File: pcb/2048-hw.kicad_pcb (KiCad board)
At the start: 2 copper layers, 60 x 93 mm, 102 parts, among them J1 UJC-HP-3-SMT-TR, J2 Battery, J3 SWD, SW1 SW_SPDT, SW2 PUSH_A, SW3 PUSH_B, U1 STM32F303K8Tx, U2 MCP73831-2-OT, U3 AP2210N-3.3TRG1, U4 PSP_1000_JSTK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

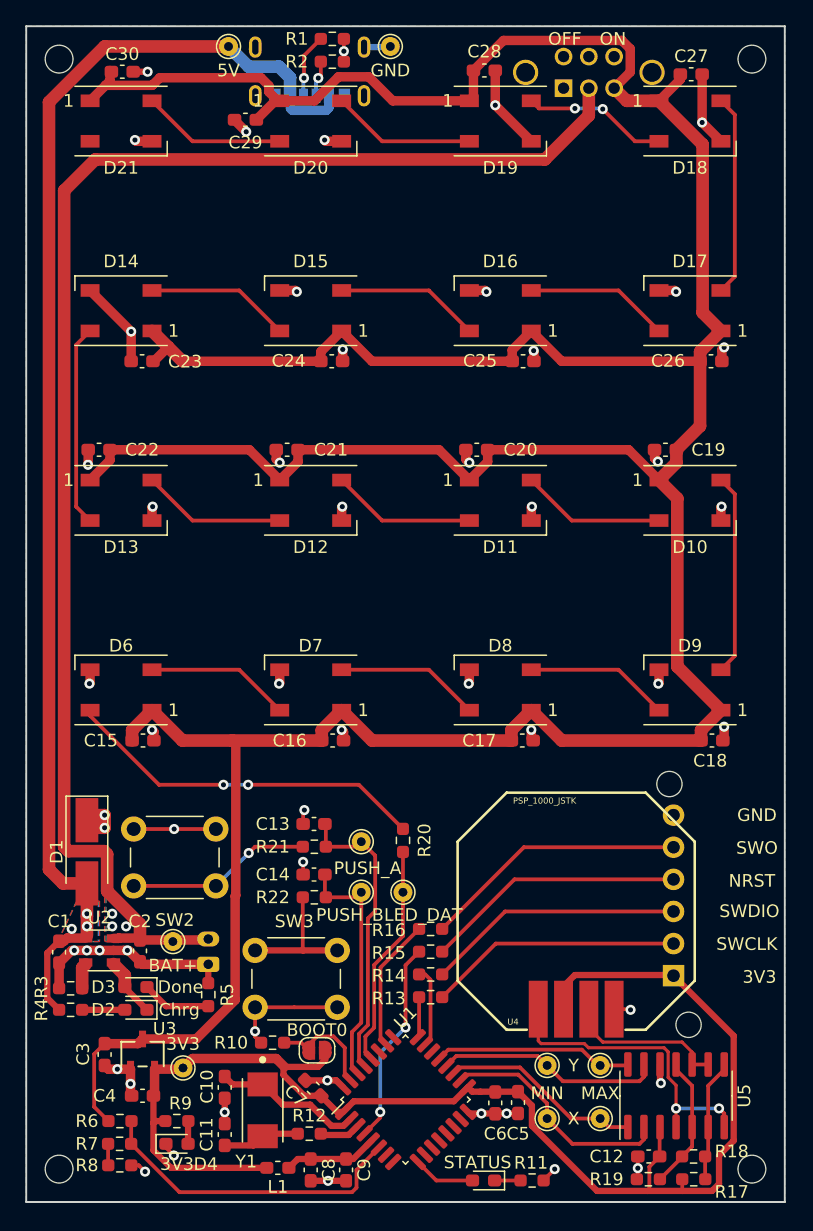
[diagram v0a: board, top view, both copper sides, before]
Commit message: Round off board corners
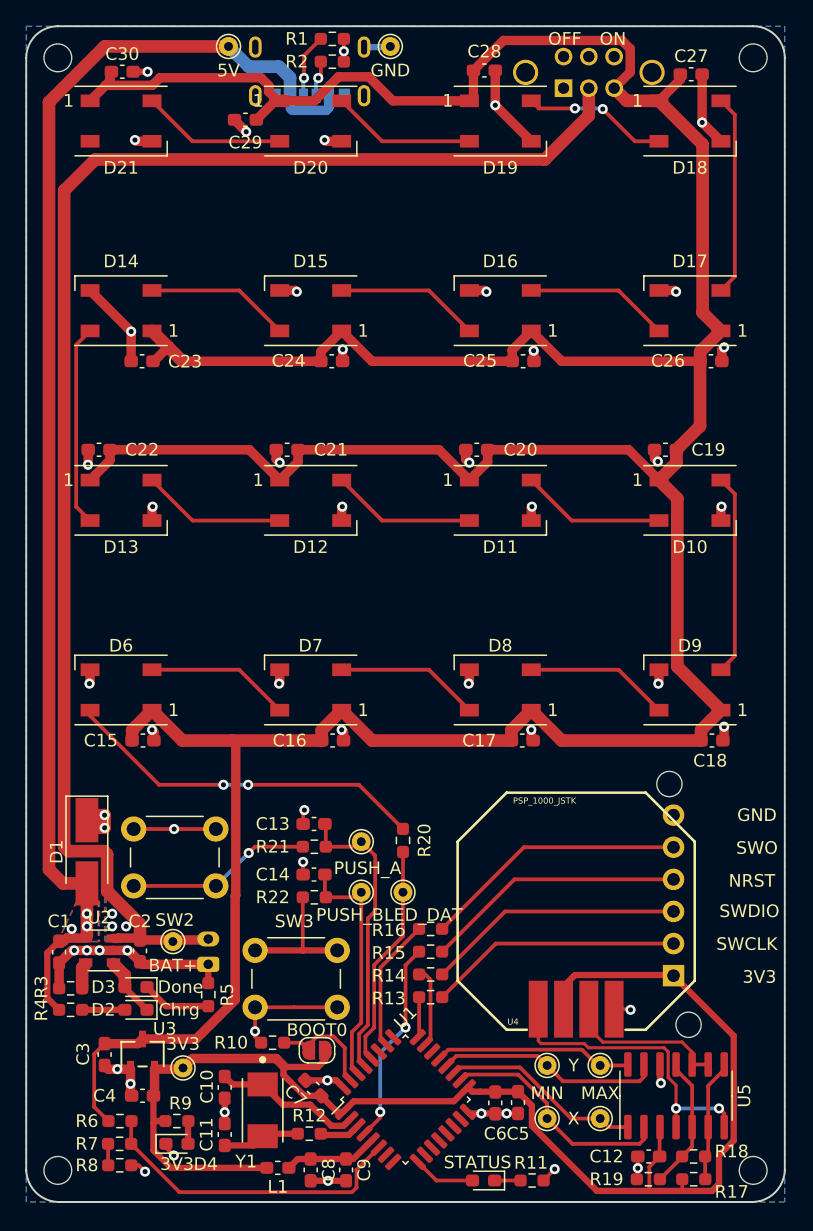
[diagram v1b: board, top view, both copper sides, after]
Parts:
- moved H1 0.14 mm to (122.5, 62.5)
- moved H3 0.14 mm to (177.5, 62.5)
- moved H2 0.14 mm to (122.5, 150.5)
- moved H4 0.14 mm to (177.5, 150.5)
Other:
- outline, holes or cut-outs redrawn
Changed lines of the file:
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@@
   (general
     (thickness 1.6)
-    (drawings 19)
+    (drawings 23)
     (tracks 594)
     (zones 0)
@@
   )
   (setup
-    (last_trace_width 0.3)
+    (last_trace_width 0.25)
     (user_trace_width 0.3)
     (user_trace_width 0.5)
@@
   )
   (module MountingHole:MountingHole_2.2mm_M2 (layer F.Cu)
-    (at 177.4 150.4)
+    (at 177.5 150.5)
     (descr "Mounting Hole 2.2mm, no annular, M2")
     (tags "mounting hole 2.2mm no annular m2")
@@
   )
   (module MountingHole:MountingHole_2.2mm_M2 (layer F.Cu)
-    (at 177.4 62.6)
+    (at 177.5 62.5)
     (descr "Mounting Hole 2.2mm, no annular, M2")
     (tags "mounting hole 2.2mm no annular m2")
@@
   )
   (module MountingHole:MountingHole_2.2mm_M2 (layer F.Cu)
-    (at 122.6 150.4)
+    (at 122.5 150.5)
     (descr "Mounting Hole 2.2mm, no annular, M2")
     (tags "mounting hole 2.2mm no annular m2")
@@
   )
   (module MountingHole:MountingHole_2.2mm_M2 (layer F.Cu)
-    (at 122.6 62.6)
+    (at 122.5 62.5)
     (descr "Mounting Hole 2.2mm, no annular, M2")
     (tags "mounting hole 2.2mm no annular m2")
@@
     )
   )
+  (gr_arc (start 122.5 62.5) (end 122.5 60) (angle -90) (layer Edge.Cuts) (width 0.15))
+  (gr_arc (start 177.5 62.5) (end 180 62.5) (angle -90) (layer Edge.Cuts) (width 0.15))
+  (gr_arc (start 122.6 150.4) (end 120 150.5) (angle -85.59480368) (layer Edge.Cuts) (width 0.15))
+  (gr_arc (start 177.4 150.4) (end 177.5 153) (angle -85.59480368) (layer Edge.Cuts) (width 0.15))
   (gr_text GND (at 177.8 122.4) (layer F.SilkS)
     (effects (font (size 1 1) (thickness 0.15)))
@@
     (effects (font (size 1 1) (thickness 0.15)))
   )
-  (gr_line (start 180 153) (end 120 153) (layer Edge.Cuts) (width 0.15))
-  (gr_line (start 180 60) (end 180 153) (layer Edge.Cuts) (width 0.15))
-  (gr_line (start 120 60) (end 180 60) (layer Edge.Cuts) (width 0.15))
-  (gr_line (start 120 153) (end 120 60) (layer Edge.Cuts) (width 0.15))
+  (gr_line (start 177.5 153) (end 122.5 153) (layer Edge.Cuts) (width 0.15))
+  (gr_line (start 180 62.5) (end 180 150.5) (layer Edge.Cuts) (width 0.15))
+  (gr_line (start 122.5 60) (end 177.5 60) (layer Edge.Cuts) (width 0.15))
+  (gr_line (start 120 150.5) (end 120 62.5) (layer Edge.Cuts) (width 0.15))
   (gr_line (start 180 120) (end 120 120) (layer Dwgs.User) (width 0.15))
   (segment (start 140.9 66.5) (end 140.9 65.5) (width 0.75) (layer B.Cu) (net 1))
@@
   (segment (start 138.1 137.6) (end 141.2 137.6) (width 0.3) (layer F.Cu) (net 2))
   (segment (start 128.5 123.5) (end 131.7 123.5) (width 0.3) (layer F.Cu) (net 2))
-  (via (at 137.4 68.35) (size 0.8) (drill 0.4) (layers F.Cu B.Cu) (net 2))
-  (segment (start 136.475 67.425) (end 137.4 68.35) (width 0.75) (layer F.Cu) (net 2))
-  (segment (start 136.475 67.4) (end 136.475 67.425) (width 0.75) (layer F.Cu) (net 2))
   (via (at 128.6 69) (size 0.8) (drill 0.4) (layers F.Cu B.Cu) (net 2))
   (segment (start 128.7 69.1) (end 128.6 69) (width 0.75) (layer F.Cu) (net 2))
@@
   (segment (start 168.375 150.325) (end 168.375 151.125) (width 0.3) (layer F.Cu) (net 2))
   (via (at 168.375 150.325) (size 0.8) (drill 0.4) (layers F.Cu B.Cu) (net 2))
+  (segment (start 136.475 67.4) (end 136.475 67.425) (width 0.75) (layer F.Cu) (net 2) (status 1000000))
+  (segment (start 136.475 67.425) (end 137.4 68.35) (width 0.75) (layer F.Cu) (net 2) (status 1000000))
+  (via (at 137.4 68.35) (size 0.8) (drill 0.4) (layers F.Cu B.Cu) (net 2) (status 1000000))
   (segment (start 128.849999 132.124999) (end 129 132.275) (width 0.75) (layer F.Cu) (net 3))
   (segment (start 127.331484 132.124999) (end 128.849999 132.124999) (width 0.75) (layer F.Cu) (net 3))
@@
   (segment (start 155.375 65.575) (end 155.05 65.9) (width 0.75) (layer F.Cu) (net 4))
   (segment (start 155.375 63.5) (end 155.375 65.575) (width 0.75) (layer F.Cu) (net 4))
-  (segment (start 139.7 65.9) (end 138.2 67.4) (width 0.75) (layer F.Cu) (net 4))
-  (segment (start 140.05 65.9) (end 139.7 65.9) (width 0.75) (layer F.Cu) (net 4))
   (segment (start 126.625 63.5) (end 126.625 64.325) (width 0.75) (layer F.Cu) (net 4))
   (segment (start 173.3 91.625) (end 171.425 93.5) (width 1) (layer F.Cu) (net 4))
@@
   (segment (start 139.9 65.9) (end 139.19501 65.19501) (width 0.75) (layer F.Cu) (net 4))
   (segment (start 126.625 64.325) (end 126.275 64.675) (width 0.75) (layer F.Cu) (net 4))
+  (segment (start 140.05 65.9) (end 139.7 65.9) (width 0.75) (layer F.Cu) (net 4) (status 1000000))
+  (segment (start 139.7 65.9) (end 138.2 67.4) (width 0.75) (layer F.Cu) (net 4) (status 1000000))
   (segment (start 144.582152 145.872272) (end 143.30988 144.6) (width 0.5) (layer F.Cu) (net 5))
   (segment (start 145.06793 145.872272) (end 144.582152 145.872272) (width 0.5) (layer F.Cu) (net 5))
@@
   (segment (start 171.8875 151.2) (end 171.8875 152.1125) (width 0.3) (layer F.Cu) (net 5))
   (segment (start 171.87499 152.12501) (end 174.247278 152.12501) (width 0.5) (layer F.Cu) (net 5))
+  (segment (start 169.12501 152.12501) (end 171.87499 152.12501) (width 0.5) (layer F.Cu) (net 5))
+  (segment (start 165.149008 152.12501) (end 169.12501 152.12501) (width 0.5) (layer F.Cu) (net 5))
   (segment (start 169.28749 151.96253) (end 169.12501 152.12501) (width 0.3) (layer F.Cu) (net 5))
   (segment (start 169.28749 150.21251) (end 169.28749 151.96253) (width 0.3) (layer F.Cu) (net 5))
   (segment (start 170.1 149.4) (end 169.28749 150.21251) (width 0.3) (layer F.Cu) (net 5))
-  (segment (start 169.12501 152.12501) (end 171.87499 152.12501) (width 0.5) (layer F.Cu) (net 5))
-  (segment (start 165.149008 152.12501) (end 169.12501 152.12501) (width 0.5) (layer F.Cu) (net 5))
   (segment (start 145.865686 149.6) (end 147.330672 148.135014) (width 0.5) (layer F.Cu) (net 6))
   (segment (start 145.3 149.6) (end 145.865686 149.6) (width 0.5) (layer F.Cu) (net 6))
@@
   (segment (start 148.15 69.1) (end 144.95 65.9) (width 0.3) (layer F.Cu) (net 29))
   (segment (start 155.05 69.1) (end 148.15 69.1) (width 0.3) (layer F.Cu) (net 29))
-  (segment (start 133.15 69.1) (end 129.95 65.9) (width 0.3) (layer F.Cu) (net 30))
-  (segment (start 140.05 69.1) (end 133.15 69.1) (width 0.3) (layer F.Cu) (net 30))
+  (segment (start 140.05 69.1) (end 133.15 69.1) (width 0.3) (layer F.Cu) (net 30) (status 1000000))
+  (segment (start 133.15 69.1) (end 129.95 65.9) (width 0.3) (layer F.Cu) (net 30) (status 1000000))
   (via (at 143.1 64.1) (size 0.8) (drill 0.4) (layers F.Cu B.Cu) (net 32))
   (segment (start 143.3 63.9) (end 143.1 64.1) (width 0.3) (layer F.Cu) (net 32))

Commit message: Use shorter power switch
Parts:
- SW1: footprint 2048-hw:E_SWITCH_EG2208A -> 2048-hw:E_SWITCH_EG2208

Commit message: Tidy up silkscreen and traces
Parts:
- D10, D11, D12, D13, D14, D15, D16, D17, D18, D19, D20, D21, D6, D7, D8, D9: footprint LED_SMD:LED_WS2812B_PLCC4_5.0x5.0mm_P3.2mm -> 2048-hw:LED_WS2812B_PLCC4_5.0x5.0mm_P3.2mm_no1
- moved C8 1.10 mm to (143.6, 150.5)
- moved D5 0.65 mm to (155.5, 151.3)
- turned C15 to 180 degrees
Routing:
- net Net-(R22-Pad2): track 17.2 -> 10.7 mm
- net GND: track 116.8 -> 120.6 mm, vias 53 -> 52
- net V_BAT: track 319.8 -> 319.0 mm
- net Net-(D5-Pad1): track 2.05 -> 2.70 mm
- net LED_STATUS: track 4.94 -> 4.29 mm
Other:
- board text added: "+"
- board text added: "-"
- board text added: "2048-hw"
- board text added: "Rev 1.0 | Christopher Hall"

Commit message: Reverse the backwards zener diode
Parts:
- turned D1 to 90 degrees
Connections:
- D1 pad 1: GND -> +5V
- D1 pad 2: +5V -> GND

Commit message: Update component values for BOM
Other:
- board text added: "JLCJLCJLCJLC"
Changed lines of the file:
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@@
   (general
     (thickness 1.6)
-    (drawings 36)
+    (drawings 37)
     (tracks 594)
     (zones 0)
@@
       (usegerberattributes true)
       (usegerberadvancedattributes true)
-      (creategerberjobfile true)
+      (creategerberjobfile false)
       (excludeedgelayer true)
       (linewidth 0.100000)
@@
       (outputformat 1)
       (mirror false)
-      (drillshape 1)
+      (drillshape 0)
       (scaleselection 1)
-      (outputdirectory ""))
+      (outputdirectory "gerber/"))
   )
   (net 0 "")
@@
       (effects (font (size 1 1) (thickness 0.15)) (justify mirror))
     )
-    (pad 1 thru_hole roundrect (at 0 0 90) (size 1.2 1.75) (drill 0.75) (layers *.Cu *.Mask) (roundrect_rratio 0.208333)
+    (pad 1 thru_hole roundrect (at 0 0 90) (size 1.2 1.75) (drill 0.75) (layers *.Cu *.Mask) (roundrect_rratio 0.2083325)
       (net 2 GND))
     (pad 2 thru_hole oval (at 2 0 90) (size 1.2 1.75) (drill 0.75) (layers *.Cu *.Mask)
@@
     )
   )
+  (gr_text JLCJLCJLCJLC (at 149.8 145) (layer F.SilkS)
+    (effects (font (size 0.7 0.7) (thickness 0.1)))
+  )
   (gr_circle (center 127.9 134.1) (end 128 134.1) (layer F.SilkS) (width 0.2))

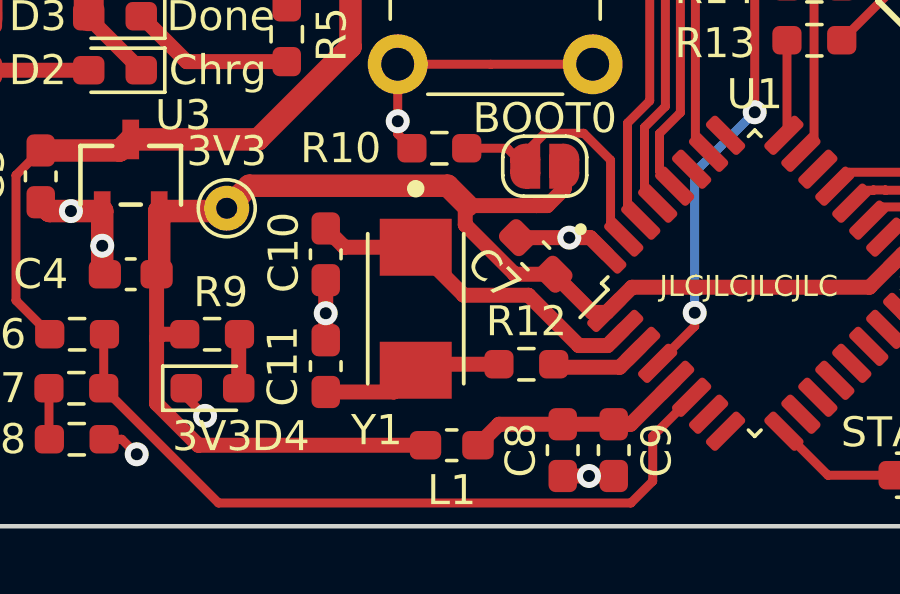
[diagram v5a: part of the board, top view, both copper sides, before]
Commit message: pcb: Remove crystal
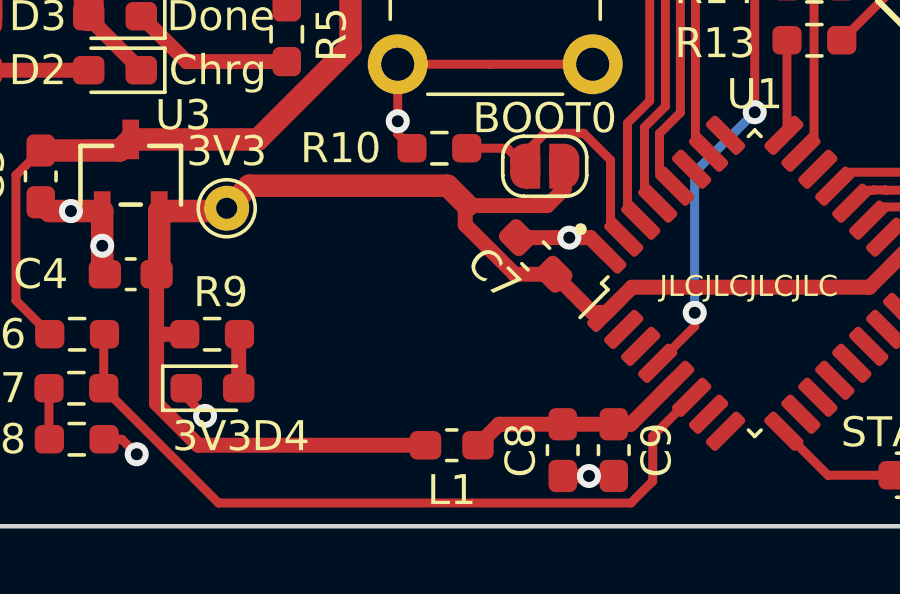
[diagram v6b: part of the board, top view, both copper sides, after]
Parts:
- removed C10, C11: 12p, Capacitor_SMD:C_0603_1608Metric_Pad1.08x0.95mm_HandSolder
- removed R12: 0, Resistor_SMD:R_0603_1608Metric_Pad0.98x0.95mm_HandSolder
- removed Y1: ECS-80-12-30Q-DS-TR, 2048-hw:XTAL_ECS-80-18-30-JGN-TR
- R21, R22: value 1k -> 2k2
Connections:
- U1 pad 2: HSE_IN -> Net-(U1-Pad2)
- U1 pad 3: HSE_OUT -> Net-(U1-Pad3)
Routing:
- net HSE_IN: track 11.8 -> 0.00 mm
- net Net-(C11-Pad1): track 6.16 -> 0.00 mm
- net HSE_OUT: track 3.23 -> 0.00 mm
- net GND: track 120.6 -> 118.6 mm, vias 52 -> 51

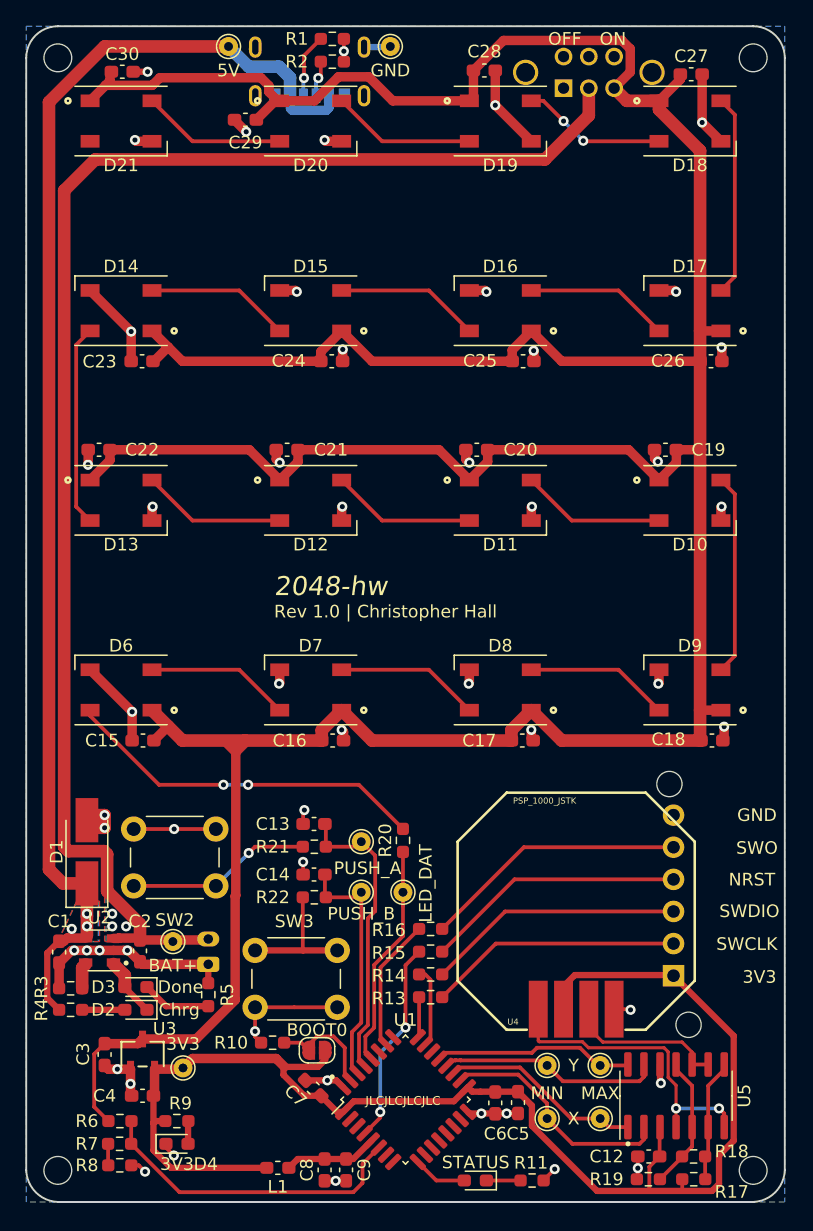
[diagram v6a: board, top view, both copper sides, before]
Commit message: pcb: Make routing changes to facilitate EEPROM
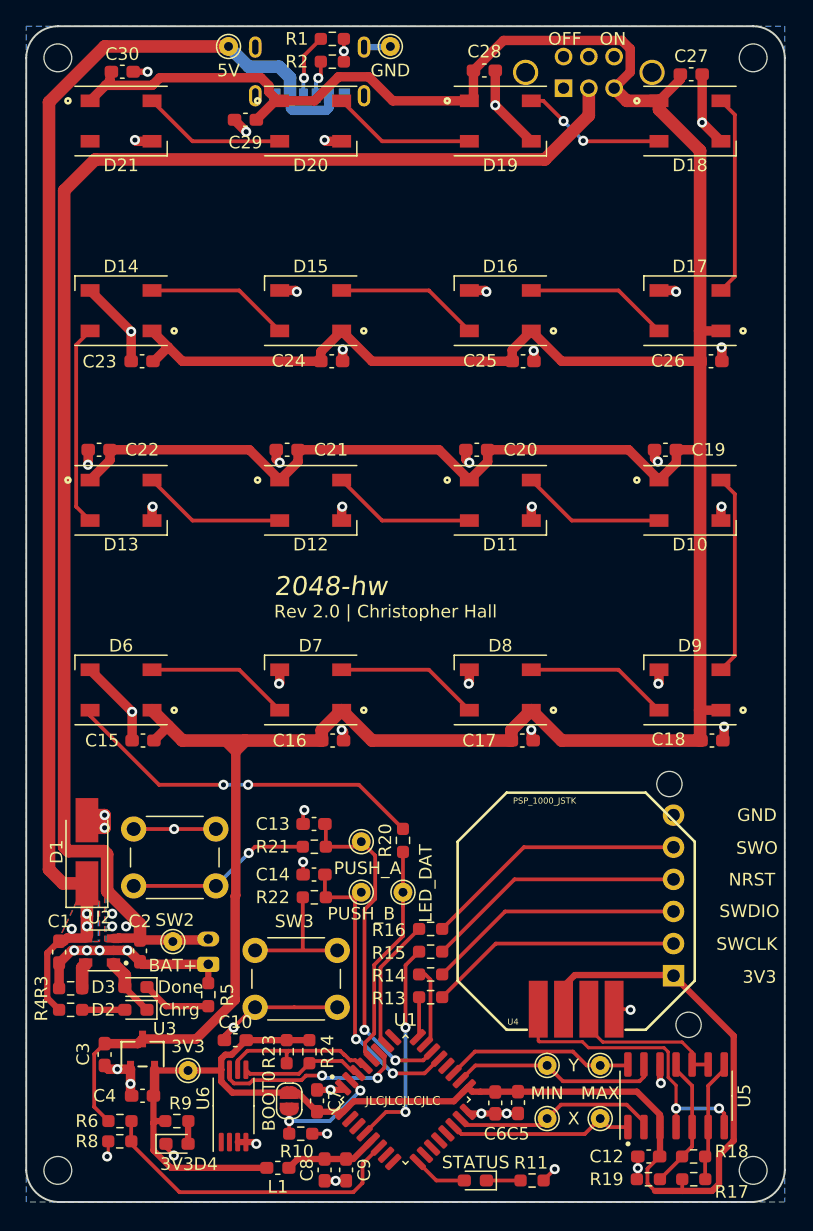
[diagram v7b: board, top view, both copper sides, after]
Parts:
- removed R7: 4k7, Resistor_SMD:R_0603_1608Metric_Pad0.98x0.95mm_HandSolder
- added C10: 100n, Capacitor_SMD:C_0603_1608Metric_Pad1.08x0.95mm_HandSolder, F.Cu at (136.5, 140.2)
- added R23: 10k, Resistor_SMD:R_0603_1608Metric_Pad0.98x0.95mm_HandSolder, F.Cu at (140.6, 141.1)
- added R24: 10k, Resistor_SMD:R_0603_1608Metric_Pad0.98x0.95mm_HandSolder, F.Cu at (142.4, 141.1)
- added U6: AT24C08D-XHM-B, Package_SO:TSSOP-8_4.4x3mm_P0.65mm, F.Cu at (136.4, 145.4)
- R8: value 4k7 -> 10k
- moved R10 7.54 mm to (141.7, 147.6), turned to 180 degrees
- moved JP1 4.57 mm to (140.8, 145.0), turned to 270 degrees
- moved R8 1.90 mm to (127.4, 148.2), turned to 0 degrees
- moved C7 1.05 mm to (143.0, 145.0), turned to 90 degrees
- moved TP4 0.45 mm to (132.8, 142.6)
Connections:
- R8 pad 2: Net-(R7-Pad1) -> BAT_ADC
- U1 pad 14: Net-(U1-Pad14) -> X_MAX
- U1 pad 15: Net-(U1-Pad15) -> X_MIN
- U1 pad 18: X_MIN -> Y_MIN
- U1 pad 19: X_MAX -> Y_MAX
- U1 pad 20: Y_MIN -> Net-(U1-Pad20)
- U1 pad 21: Y_MAX -> PUSH_B
- U1 pad 22: Net-(U1-Pad22) -> PUSH_A
- U1 pad 27: Net-(U1-Pad27) -> EEPROM_WP
- U1 pad 29: PUSH_A -> I2C_SCL
- U1 pad 30: PUSH_B -> I2C_SDA
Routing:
- net EEPROM_WP: track 0.00 -> 15.4 mm, vias 0 -> 2
- net I2C_SCL: track 0.00 -> 12.6 mm
- net I2C_SDA: track 0.00 -> 9.77 mm
- net PUSH_B: track 19.6 -> 24.8 mm, vias 0 -> 2
- net PUSH_A: track 23.7 -> 27.1 mm, vias 0 -> 2
- net X_MIN: track 18.8 -> 16.3 mm
- net GND: track 118.6 -> 120.7 mm, vias 51 -> 53
- net Net-(R7-Pad1): track 1.71 -> 0.00 mm
- net +3V3: track 110.6 -> 111.9 mm
- net X_MAX: track 15.9 -> 14.8 mm
- net Y_MIN: track 17.6 -> 16.6 mm
- net Y_MAX: track 15.9 -> 15.0 mm
- net NRST: track 16.2 -> 17.1 mm
- net BOOT0: track 8.88 -> 9.73 mm, vias 0 -> 2
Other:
- board text added: "Rev 2.0 | Christopher Hall"
- board text removed: "Rev 1.0 | Christopher Hall"
